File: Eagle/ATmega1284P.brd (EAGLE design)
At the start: 53.3 x 25.4 mm, 32 parts, among them IC1 ATMEGA644A, IC3 LM336LP, IC4 LM1117

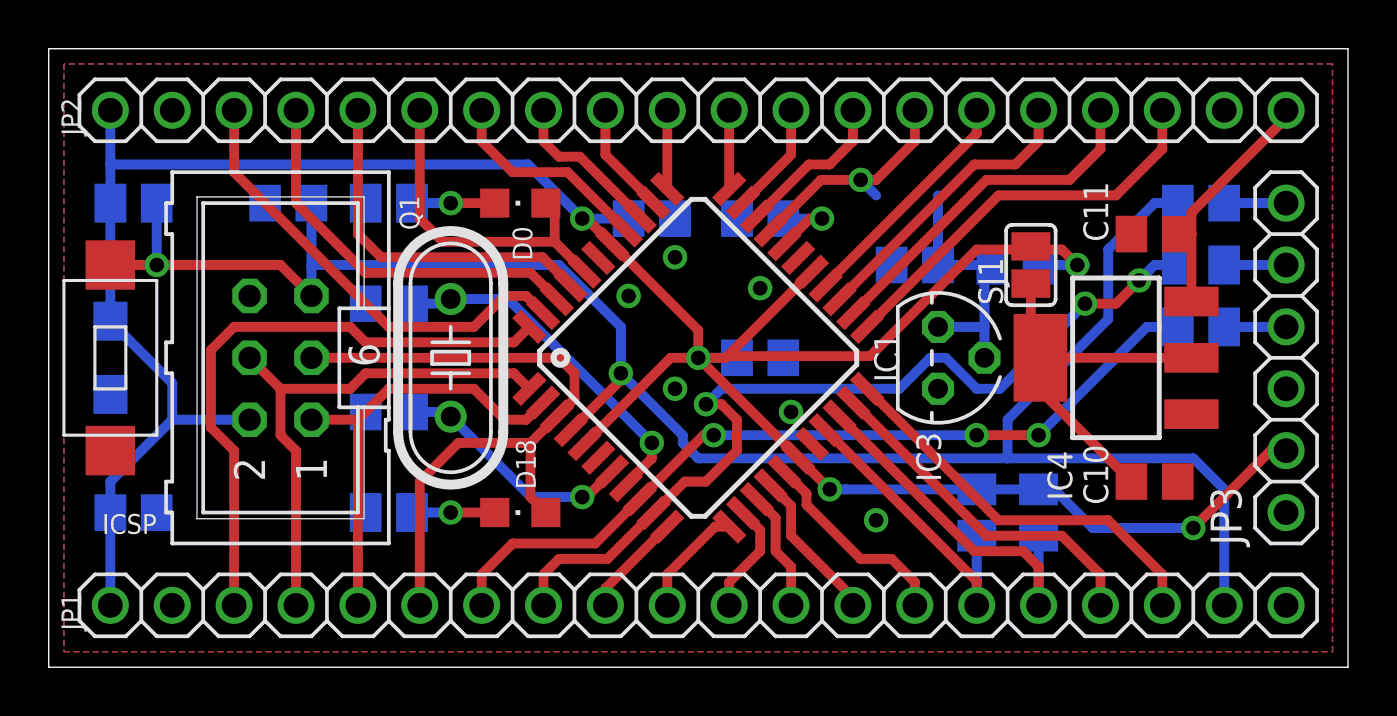
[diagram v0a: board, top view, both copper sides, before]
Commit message: Changed voltage reference to LM4040 Changed THT crystal to SMT resonator Added a few capacitors
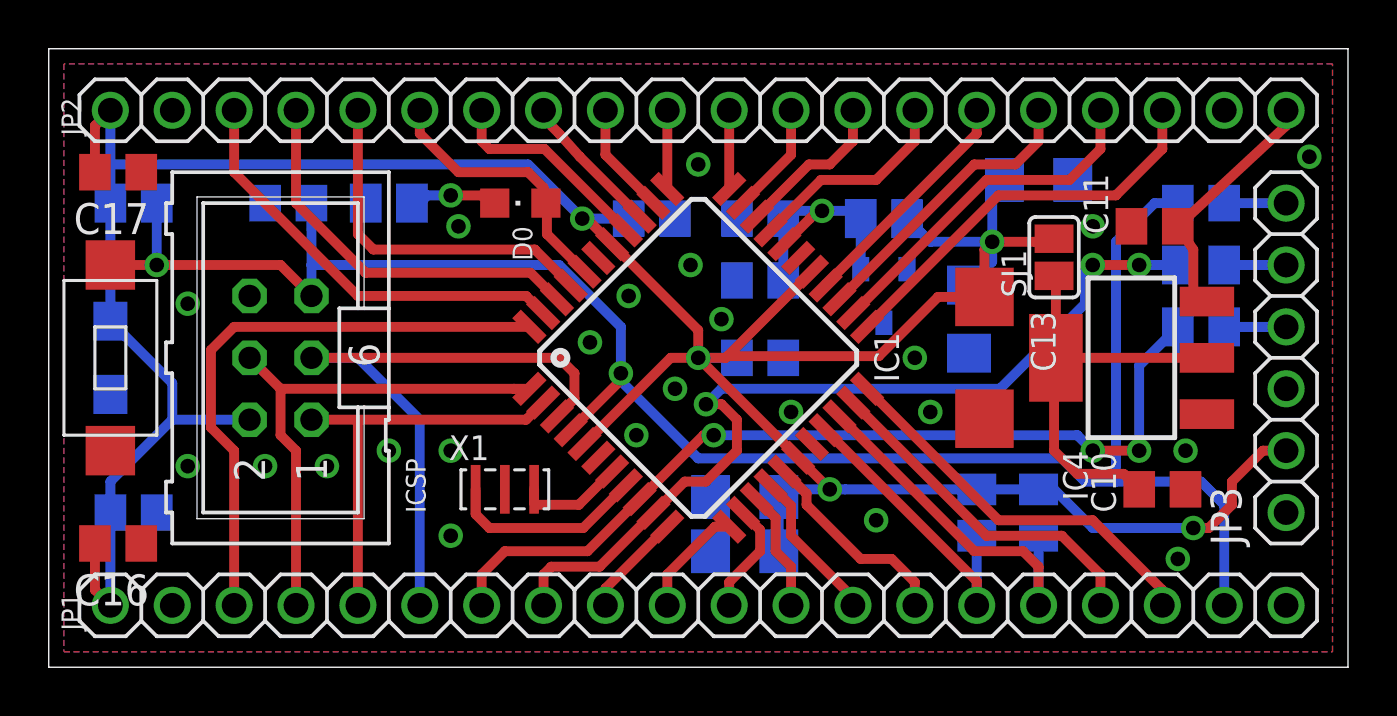
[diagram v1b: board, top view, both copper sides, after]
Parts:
- removed D18: (no value), led:CHIPLED_0805
- removed IC3: LM336LP, linear:TO92
- removed Q1: (no value), crystal:HC49/S
- removed R9: 1K6, rcl:M0805
- added C13: (no value), rcl:SMC_C
- added C14, C15: 100u, rcl:C1206
- added C16, C17: 100n, rcl:C0805
- added IC2: LM4040, texas:DBZ_R-PDSO-G3
- added X1: 8Mhz, SteMarie:CERALOCK_CSTCE_G
- C1, C2: value 22p -> 100u; device rcl:C0805 -> rcl:C1206
- moved C1 24.1 mm to (37.8, 14.3), turned to 270 degrees
- moved C2 16.6 mm to (28.6, 6.99), turned to 0 degrees
- moved C12 6.38 mm to (29.2, 15.9)
- moved R4 5.72 mm to (34.3, 18.4)
- moved SJ1 1.00 mm to (41.3, 16.8)
- moved IC4 0.64 mm to (44.5, 12.7)
- moved C10 0.45 mm to (45.7, 7.30)
- moved C11 0.32 mm to (45.4, 18.1)
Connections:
- removed net N$31: C1.2, IC1.7, Q1.2
- removed net N$32: C2.2, IC1.8, Q1.1
- removed net N$5: D18.C, R9.2
- new net N$3: IC1.7, X1.P$3
- new net N$4: IC1.8, X1.P$1
- net AREF: now also IC2.1; no longer IC3.1, IC3.2
- net GND: now also C1.2, C13.-, C14.2, C15.2, C16.1, C17.1, C2.2, IC2.2, X1.P$2; no longer C1.1, C2.1, IC3.3, R9.1
- net PB7: no longer D18.A
- net VCC: now also C1.1, C13.+, C14.1, C15.1, C16.2, C17.2, C2.1
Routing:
- net VCC: track 116.9 -> 134.7 mm
- net N$32: track 14.6 -> 0.00 mm, vias 1 -> 0
- net N$31: track 10.1 -> 0.00 mm, vias 1 -> 0
- net N$4: track 0.00 -> 8.15 mm
- net N$3: track 0.00 -> 4.36 mm
- net AREF: track 14.5 -> 10.4 mm
- net PD0: track 34.1 -> 37.6 mm
- net N$5: track 3.40 -> 0.00 mm, vias 1 -> 0
- net PB0: track 13.8 -> 11.1 mm
- net N$6: track 16.0 -> 18.6 mm
- net PB7: track 28.1 -> 26.2 mm
- net /RESET: track 79.6 -> 78.3 mm
- net PB6: track 18.5 -> 17.4 mm
- net PB3: track 18.7 -> 17.6 mm
- net PA7: track 9.60 -> 8.71 mm, vias 1 -> 0
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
